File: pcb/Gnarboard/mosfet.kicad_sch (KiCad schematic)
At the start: 12 parts, among them Q1 IRF4905, Q2 MMBT5551L, U5 ACS725xLCTR-20AU

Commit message: board close to being ready for a prototype
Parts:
- added J5: Screw_Terminal_01x02, gnarboard:Amphenol OQ02715, symbol Connector:Screw_Terminal_01x02
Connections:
- net LOAD+: no longer names the net of F1.3, Q1.2 (D)
- net LOAD+: now also J5.1 (Pin_1)
- net LOAD-: no longer names the net of U5.1 (IP+), U5.2 (IP+)
- net LOAD-: now also J5.2 (Pin_2)
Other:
- moved on the sheet: C3, C4, C5, U5

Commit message: added the flyback diode
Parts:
- added D10: GS1G-LTP, Diode_SMD:D_SMA, symbol Diode:MRA4004T3G
- R4: value 10k -> 47k
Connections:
- net at F1.3, J5.1 (Pin_1), Q1.2 (D): now also D10.1 (K)
- net at J5.2 (Pin_2), U5.1 (IP+), U5.2 (IP+): now also D10.2 (A)
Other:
- moved on the sheet: J5
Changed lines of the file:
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@@
   (junction (at 167.64 113.03) (diameter 0) (color 0 0 0 0)
   )
+  (junction (at 148.59 86.36) (diameter 0) (color 0 0 0 0)
+  )
   (junction (at 107.95 76.2) (diameter 0) (color 0 0 0 0)
   )
@@
   (junction (at 139.7 72.39) (diameter 0) (color 0 0 0 0)
   )
+  (junction (at 148.59 83.82) (diameter 0) (color 0 0 0 0)
+  )
   (junction (at 139.7 54.61) (diameter 0) (color 0 0 0 0)
   )
@@
     (stroke (width 0) (type default))
   )
-  (wire (pts (xy 139.7 87.63) (xy 149.86 87.63))
+  (wire (pts (xy 139.7 83.82) (xy 148.59 83.82))
     (stroke (width 0) (type default))
   )
@@
     (stroke (width 0) (type default))
   )
-  (wire (pts (xy 139.7 90.17) (xy 139.7 107.95))
-    (stroke (width 0) (type default))
-  )
-  (wire (pts (xy 149.86 90.17) (xy 139.7 90.17))
+  (wire (pts (xy 139.7 86.36) (xy 139.7 107.95))
+    (stroke (width 0) (type default))
+  )
+  (wire (pts (xy 149.86 86.36) (xy 148.59 86.36))
     (stroke (width 0) (type default))
   )
@@
     (stroke (width 0) (type default))
   )
-  (wire (pts (xy 139.7 72.39) (xy 139.7 87.63))
+  (wire (pts (xy 139.7 72.39) (xy 139.7 83.82))
     (stroke (width 0) (type default))
   )
@@
     (stroke (width 0) (type default))
   )
+  (wire (pts (xy 148.59 80.01) (xy 148.59 83.82))
+    (stroke (width 0) (type default))
+  )
+  (wire (pts (xy 162.56 88.9) (xy 162.56 90.17))
+    (stroke (width 0) (type default))
+  )
   (wire (pts (xy 127 91.44) (xy 118.11 91.44))
     (stroke (width 0) (type default))
@@
     (stroke (width 0) (type default))
   )
+  (wire (pts (xy 148.59 90.17) (xy 148.59 86.36))
+    (stroke (width 0) (type default))
+  )
+  (wire (pts (xy 162.56 90.17) (xy 148.59 90.17))
+    (stroke (width 0) (type default))
+  )
   (wire (pts (xy 160.02 124.46) (xy 167.64 124.46))
     (stroke (width 0) (type default))
@@
     (stroke (width 0) (type default))
   )
+  (wire (pts (xy 148.59 86.36) (xy 139.7 86.36))
+    (stroke (width 0) (type default))
+  )
   (wire (pts (xy 116.84 76.2) (xy 119.38 76.2))
     (stroke (width 0) (type default))
@@
     (stroke (width 0) (type default))
   )
+  (wire (pts (xy 162.56 81.28) (xy 162.56 80.01))
+    (stroke (width 0) (type default))
+  )
   (wire (pts (xy 128.27 62.23) (xy 128.27 63.5))
     (stroke (width 0) (type default))
@@
     (stroke (width 0) (type default))
   )
+  (wire (pts (xy 162.56 80.01) (xy 148.59 80.01))
+    (stroke (width 0) (type default))
+  )
   (wire (pts (xy 128.27 71.12) (xy 128.27 69.85))
     (stroke (width 0) (type default))
@@
   )
   (wire (pts (xy 160.02 113.03) (xy 167.64 113.03))
+    (stroke (width 0) (type default))
+  )
+  (wire (pts (xy 148.59 83.82) (xy 149.86 83.82))
     (stroke (width 0) (type default))
   )
@@
     )
   )
+  (symbol (lib_id "Diode:MRA4004T3G") (at 162.56 85.09 270) (unit 1)
+    (in_bom yes) (on_board yes) (dnp no) (fields_autoplaced)
+    (property "Reference" "D10" (at 165.1 83.82 90)
+      (effects (font (size 1.27 1.27)) (justify left))
+    )
+    (property "Value" "GS1G-LTP" (at 165.1 86.36 90)
+      (effects (font (size 1.27 1.27)) (justify left))
+    )
+    (property "Footprint" "Diode_SMD:D_SMA" (at 158.115 85.09 0)
+      (effects (font (size 1.27 1.27)) hide)
+    )
+    (property "Datasheet" "http://www.onsemi.com/pub_link/Collateral/MRA4003T3-D.PDF" (at 162.56 85.09 0)
+      (effects (font (size 1.27 1.27)) hide)
+    )
+    (property "Sim.Device" "D" (at 162.56 85.09 0)
+      (effects (font (size 1.27 1.27)) hide)
+    )
+    (property "Sim.Pins" "1=K 2=A" (at 162.56 85.09 0)
+      (effects (font (size 1.27 1.27)) hide)
+    )
+    (pin "1")
+    (pin "2")
+    (instances
+      (project "Gnarboard"
+        (path "/c83c6236-96e9-46ad-9d7a-9e2efa4a7966/0eec6767-666b-42c0-ba36-2a83c9caeade"
+          (reference "D10") (unit 1)
+        )
+        (path "/c83c6236-96e9-46ad-9d7a-9e2efa4a7966/ccdb1c25-8d0f-4f30-ab70-bbc1ecf3f6f7"
+          (reference "D11") (unit 1)
+        )
+        (path "/c83c6236-96e9-46ad-9d7a-9e2efa4a7966/1e692482-a022-407a-8cb5-d9a3b23521a6"
+          (reference "D12") (unit 1)
+        )
+        (path "/c83c6236-96e9-46ad-9d7a-9e2efa4a7966/5952e660-2bb6-45cf-b9ea-f7a7c2d0954e"
+          (reference "D13") (unit 1)
+        )
+        (path "/c83c6236-96e9-46ad-9d7a-9e2efa4a7966/772d44f5-8758-48db-a140-72ed8e75e88c"
+          (reference "D14") (unit 1)
+        )
+        (path "/c83c6236-96e9-46ad-9d7a-9e2efa4a7966/424e7b24-5644-46f2-85bb-1e459a343705"
+          (reference "D15") (unit 1)
+        )
+        (path "/c83c6236-96e9-46ad-9d7a-9e2efa4a7966/4c1df725-56ca-4be4-8107-a39054acbca4"
+          (reference "D16") (unit 1)
+        )
+        (path "/c83c6236-96e9-46ad-9d7a-9e2efa4a7966/a8a81147-5613-4820-beb3-a7ca76d0db8e"
+          (reference "D17") (unit 1)
+        )
+      )
+    )
+  )
   (symbol (lib_id "Device:R_Small_US") (at 107.95 80.01 180) (unit 1)
     (in_bom yes) (on_board yes) (dnp no) (fields_autoplaced)
@@
       (effects (font (size 1.27 1.27)) (justify right))
     )
-    (property "Value" "10k" (at 130.81 60.96 0)
+    (property "Value" "47k" (at 130.81 60.96 0)
       (effects (font (size 1.27 1.27)) (justify right))
     )
@@
     )
   )
-  (symbol (lib_id "Connector:Screw_Terminal_01x02") (at 154.94 87.63 0) (unit 1)
-    (in_bom yes) (on_board yes) (dnp no) (fields_autoplaced)
-    (property "Reference" "J5" (at 157.48 87.63 0)
-      (effects (font (size 1.27 1.27)) (justify left))
-    )
-    (property "Value" "Screw_Terminal_01x02" (at 157.48 90.17 0)
+  (symbol (lib_id "Connector:Screw_Terminal_01x02") (at 154.94 83.82 0) (unit 1)
+    (in_bom yes) (on_board yes) (dnp no) (fields_autoplaced)
+    (property "Reference" "J5" (at 157.48 83.82 0)
+      (effects (font (size 1.27 1.27)) (justify left))
+    )
+    (property "Value" "Screw_Terminal_01x02" (at 157.48 86.36 0)
       (effects (font (size 1.27 1.27)) (justify left) hide)
     )
-    (property "Footprint" "gnarboard:Amphenol OQ02715" (at 154.94 87.63 0)
-      (effects (font (size 1.27 1.27)) hide)
-    )
-    (property "Datasheet" "~" (at 154.94 87.63 0)
-      (effects (font (size 1.27 1.27)) hide)
-    )
+    (property "Footprint" "gnarboard:Amphenol OQ02715" (at 154.94 83.82 0)
+      (effects (font (size 1.27 1.27)) hide)
+    )
+    (property "Datasheet" "~" (at 154.94 83.82 0)
+      (effects (font (size 1.27 1.27)) hide)
+    )

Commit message: bill of materials updated.
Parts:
- C3: Vendor (none) -> C0805C102J1HACTU
- C4: Vendor (none) -> C0805C472K5RAC
- C5: Vendor (none) -> 08053C104KAT4A
- D10, F1: Vendor (none) -> 833-GS1G-LTP
- D2: Vendor (none) -> 150080RS75000
- J5: Vendor (none) -> OQ0271500000G, TJ0271500000G
- Q1: Vendor (none) -> 942-IRF4905STRLPBF
- Q2: Vendor (none) -> 637-MMBT5551
- R1: Vendor (none) -> 652-CR0805JW-103ELF
- R2: Vendor (none) -> 652-CR0805JW-102ELF
- R3: Vendor (none) -> 652-CR0805JW-104ELF
- R4: Vendor (none) -> 652-CR0805JW-473ELF
- U5: Vendor (none) -> 250-725LLCTR20AUT
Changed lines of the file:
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@@
+      (effects (font (size 1.27 1.27)) hide)
+    )
+    (property "Vendor" " 652-CR0805JW-103ELF " (at 114.3 76.2 0)
       (effects (font (size 1.27 1.27)) hide)
     )
@@
     )
     (property "Sim.Pins" "1=K 2=A" (at 162.56 85.09 0)
+      (effects (font (size 1.27 1.27)) hide)
+    )
+    (property "Vendor" "833-GS1G-LTP" (at 162.56 85.09 0)
       (effects (font (size 1.27 1.27)) hide)
     )
@@
       (effects (font (size 1.27 1.27)) hide)
     )
+    (property "Vendor" " 652-CR0805JW-102ELF " (at 107.95 80.01 0)
+      (effects (font (size 1.27 1.27)) hide)
+    )
     (pin "1")
     (pin "2")
@@
       (effects (font (size 1.27 1.27)) hide)
     )
+    (property "Vendor" "652-CR0805JW-473ELF" (at 128.27 59.69 0)
+      (effects (font (size 1.27 1.27)) hide)
+    )
     (pin "1")
     (pin "2")
@@
     )
     (property "Datasheet" "~" (at 153.67 60.96 0)
+      (effects (font (size 1.27 1.27)) hide)
+    )
+    (property "Vendor" "833-GS1G-LTP" (at 154.94 64.77 0)
       (effects (font (size 1.27 1.27)) hide)
     )
@@
       (effects (font (size 1.27 1.27)) hide)
     )
+    (property "Vendor" "150080RS75000" (at 107.95 86.36 0)
+      (effects (font (size 1.27 1.27)) hide)
+    )
     (pin "1")
     (pin "2")
@@
       (effects (font (size 1.27 1.27)) hide)
     )
+    (property "Vendor" "08053C104KAT4A" (at 167.64 106.68 0)
+      (effects (font (size 1.27 1.27)) hide)
+    )
     (pin "1")
     (pin "2")
@@
     )
     (property "Datasheet" "~" (at 167.64 119.38 0)
+      (effects (font (size 1.27 1.27)) hide)
+    )
+    (property "Vendor" "C0805C472K5RAC" (at 167.64 119.38 0)
       (effects (font (size 1.27 1.27)) hide)
     )
@@
       (effects (font (size 1.27 1.27)) hide)
     )
+    (property "Vendor" "OQ0271500000G, TJ0271500000G" (at 154.94 83.82 0)
+      (effects (font (size 1.27 1.27)) hide)
+    )
     (pin "1")
     (pin "2")
@@
     )
     (property "Datasheet" "http://www.allegromicro.com/~/media/Files/Datasheets/ACS725-Datasheet.ashx?la=en" (at 149.86 113.03 0)
+      (effects (font (size 1.27 1.27)) hide)
+    )
+    (property "Vendor" "250-725LLCTR20AUT" (at 149.86 113.03 0)
       (effects (font (size 1.27 1.27)) hide)
     )
@@
       (effects (font (size 1.27 1.27)) hide)
     )
+    (property "Vendor" "652-CR0805JW-104ELF" (at 128.27 67.31 0)
+      (effects (font (size 1.27 1.27)) hide)
+    )
     (pin "1")
     (pin "2")
@@
     )
     (property "Datasheet" "~" (at 160.02 119.38 0)
+      (effects (font (size 1.27 1.27)) hide)
+    )
+    (property "Vendor" "C0805C102J1HACTU" (at 160.02 119.38 0)
       (effects (font (size 1.27 1.27)) hide)
     )
@@
       (effects (font (size 1.27 1.27)) (justify left) hide)
     )
+    (property "Vendor" " 942-IRF4905STRLPBF " (at 137.16 63.5 0)
+      (effects (font (size 1.27 1.27)) hide)
+    )
     (pin "1")
     (pin "2")
@@
       (effects (font (size 1.27 1.27)) (justify left) hide)
     )
-    (pin "1")
+    (property "Vendor" "637-MMBT5551" (at 124.46 76.2 0)
+      (effects (font (size 1.27 1.27)) hide)
+    )
+    (pin "1")

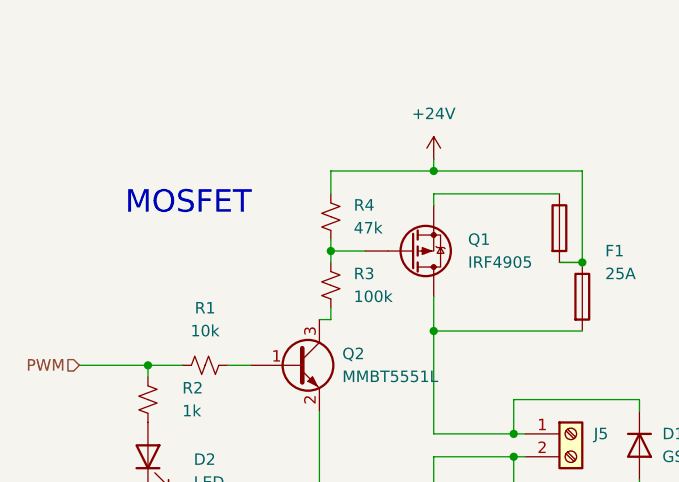
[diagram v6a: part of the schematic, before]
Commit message: got the mosfet driver circuit sorted - zener to the rescue.  also added the CAN/N2K header.
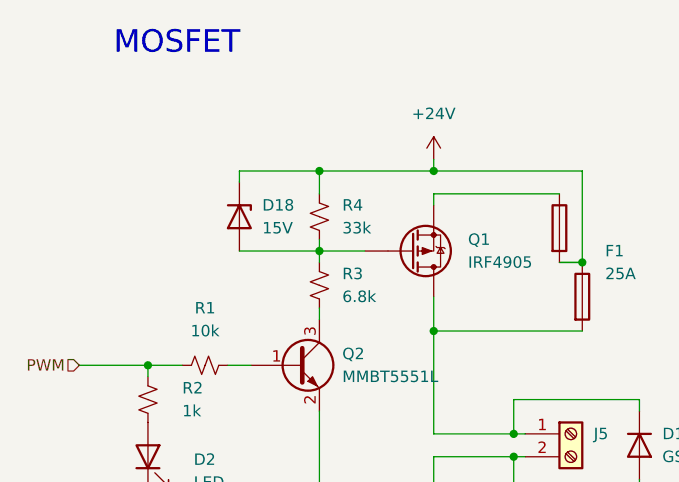
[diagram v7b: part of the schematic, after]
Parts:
- added D18: 15V, Diode_SMD:D_SOD-323_HandSoldering, symbol Device:D_Zener
- R3: value 100k -> 6.8k
- R4: value 47k -> 33k
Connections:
- net +24V: now also D18.1 (K)
- net at Q1.1 (G), R3.2, R4.1: now also D18.2 (A)
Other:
- moved on the sheet: R3, R4
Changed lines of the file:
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@@
   (junction (at 148.59 83.82) (diameter 0) (color 0 0 0 0)
   )
+  (junction (at 127 54.61) (diameter 0) (color 0 0 0 0)
+  )
   (junction (at 139.7 54.61) (diameter 0) (color 0 0 0 0)
   )
-  (junction (at 128.27 63.5) (diameter 0) (color 0 0 0 0)
+  (junction (at 127 63.5) (diameter 0) (color 0 0 0 0)
   )
   (wire (pts (xy 160.02 115.57) (xy 160.02 116.84))
@@
     (stroke (width 0) (type default))
   )
-  (wire (pts (xy 128.27 57.15) (xy 128.27 54.61))
+  (wire (pts (xy 127 57.15) (xy 127 54.61))
     (stroke (width 0) (type default))
   )
@@
     (stroke (width 0) (type default))
   )
-  (wire (pts (xy 128.27 71.12) (xy 127 71.12))
-    (stroke (width 0) (type default))
-  )
   (wire (pts (xy 161.29 102.87) (xy 161.29 106.68))
     (stroke (width 0) (type default))
@@
     (stroke (width 0) (type default))
   )
-  (wire (pts (xy 128.27 63.5) (xy 128.27 64.77))
+  (wire (pts (xy 127 63.5) (xy 127 64.77))
     (stroke (width 0) (type default))
   )
@@
     (stroke (width 0) (type default))
   )
-  (wire (pts (xy 128.27 63.5) (xy 132.08 63.5))
+  (wire (pts (xy 127 63.5) (xy 132.08 63.5))
     (stroke (width 0) (type default))
   )
@@
     (stroke (width 0) (type default))
   )
-  (wire (pts (xy 128.27 54.61) (xy 139.7 54.61))
+  (wire (pts (xy 127 54.61) (xy 139.7 54.61))
+    (stroke (width 0) (type default))
+  )
+  (wire (pts (xy 118.11 54.61) (xy 118.11 55.88))
     (stroke (width 0) (type default))
   )
@@
     (stroke (width 0) (type default))
   )
-  (wire (pts (xy 128.27 62.23) (xy 128.27 63.5))
+  (wire (pts (xy 127 62.23) (xy 127 63.5))
     (stroke (width 0) (type default))
   )
@@
     (stroke (width 0) (type default))
   )
+  (wire (pts (xy 127 54.61) (xy 118.11 54.61))
+    (stroke (width 0) (type default))
+  )
   (wire (pts (xy 162.56 80.01) (xy 148.59 80.01))
     (stroke (width 0) (type default))
   )
-  (wire (pts (xy 128.27 71.12) (xy 128.27 69.85))
+  (wire (pts (xy 127 71.12) (xy 127 69.85))
+    (stroke (width 0) (type default))
+  )
+  (wire (pts (xy 118.11 63.5) (xy 127 63.5))
     (stroke (width 0) (type default))
   )
@@
     (effects (font (size 2.5 2.5)) (justify left bottom))
   )
-  (text "MOSFET" (at 105.41 59.69 0)
+  (text "MOSFET" (at 104.14 41.91 0)
     (effects (font (size 2.5 2.5)) (justify left bottom))
   )
@@
     )
   )
-  (symbol (lib_id "Device:R_Small_US") (at 128.27 59.69 180) (unit 1)
-    (in_bom yes) (on_board yes) (dnp no) (fields_autoplaced)
-    (property "Reference" "R4" (at 130.81 58.42 0)
+  (symbol (lib_id "Device:R_Small_US") (at 127 59.69 180) (unit 1)
+    (in_bom yes) (on_board yes) (dnp no) (fields_autoplaced)
+    (property "Reference" "R4" (at 129.54 58.42 0)
       (effects (font (size 1.27 1.27)) (justify right))
     )
-    (property "Value" "47k" (at 130.81 60.96 0)
+    (property "Value" "33k" (at 129.54 60.96 0)
       (effects (font (size 1.27 1.27)) (justify right))
     )
-    (property "Footprint" "Resistor_SMD:R_0805_2012Metric_Pad1.20x1.40mm_HandSolder" (at 128.27 59.69 0)
-      (effects (font (size 1.27 1.27)) hide)
-    )
-    (property "Datasheet" "~" (at 128.27 59.69 0)
-      (effects (font (size 1.27 1.27)) hide)
-    )
-    (property "Vendor" "652-CR0805JW-473ELF" (at 128.27 59.69 0)
+    (property "Footprint" "Resistor_SMD:R_0805_2012Metric_Pad1.20x1.40mm_HandSolder" (at 127 59.69 0)
+      (effects (font (size 1.27 1.27)) hide)
+    )
+    (property "Datasheet" "~" (at 127 59.69 0)
+      (effects (font (size 1.27 1.27)) hide)
+    )
+    (property "Vendor" "652-CR0805JW-473ELF" (at 127 59.69 0)
       (effects (font (size 1.27 1.27)) hide)
     )
@@
     )
   )
-  (symbol (lib_id "Device:R_Small_US") (at 128.27 67.31 180) (unit 1)
-    (in_bom yes) (on_board yes) (dnp no) (fields_autoplaced)
-    (property "Reference" "R3" (at 130.81 66.04 0)
+  (symbol (lib_id "Device:R_Small_US") (at 127 67.31 180) (unit 1)
+    (in_bom yes) (on_board yes) (dnp no) (fields_autoplaced)
+    (property "Reference" "R3" (at 129.54 66.04 0)
       (effects (font (size 1.27 1.27)) (justify right))
     )
-    (property "Value" "100k" (at 130.81 68.58 0)
+    (property "Value" "6.8k" (at 129.54 68.58 0)
       (effects (font (size 1.27 1.27)) (justify right))
     )
-    (property "Footprint" "Resistor_SMD:R_0805_2012Metric_Pad1.20x1.40mm_HandSolder" (at 128.27 67.31 0)
-      (effects (font (size 1.27 1.27)) hide)
-    )
-    (property "Datasheet" "~" (at 128.27 67.31 0)
-      (effects (font (size 1.27 1.27)) hide)
-    )
-    (property "Vendor" "652-CR0805JW-104ELF" (at 128.27 67.31 0)
+    (property "Footprint" "Resistor_SMD:R_0805_2012Metric_Pad1.20x1.40mm_HandSolder" (at 127 67.31 0)
+      (effects (font (size 1.27 1.27)) hide)
+    )
+    (property "Datasheet" "~" (at 127 67.31 0)
+      (effects (font (size 1.27 1.27)) hide)
+    )
+    (property "Vendor" "652-CR0805JW-104ELF" (at 127 67.31 0)
       (effects (font (size 1.27 1.27)) hide)
     )
@@
         )
       )
+    )
+  )
+  (symbol (lib_id "Device:D_Zener") (at 118.11 59.69 270) (unit 1)
+    (in_bom yes) (on_board yes) (dnp no) (fields_autoplaced)
+    (property "Reference" "D18" (at 120.65 58.42 90)
+      (effects (font (size 1.27 1.27)) (justify left))
+    )
+    (property "Value" "15V" (at 120.65 60.96 90)
+      (effects (font (size 1.27 1.27)) (justify left))
+    )
+    (property "Footprint" "Diode_SMD:D_SOD-323_HandSoldering" (at 118.11 59.69 0)
+      (effects (font (size 1.27 1.27)) hide)
+    )
+    (property "Datasheet" "~" (at 118.11 59.69 0)
+      (effects (font (size 1.27 1.27)) hide)
+    )
+    (property "Vendor" "771-BZX384-C15115" (at 118.11 59.69 90)
+      (effects (font (size 1.27 1.27)) hide)
+    )
+    (pin "1")
+    (pin "2")
+    (instances
+      (project "Gnarboard"
+        (path "/c83c6236-96e9-46ad-9d7a-9e2efa4a7966/0eec6767-666b-42c0-ba36-2a83c9caeade"
+          (reference "D18") (unit 1)
+        )
+        (path "/c83c6236-96e9-46ad-9d7a-9e2efa4a7966/ccdb1c25-8d0f-4f30-ab70-bbc1ecf3f6f7"
+          (reference "D19") (unit 1)
+        )
+        (path "/c83c6236-96e9-46ad-9d7a-9e2efa4a7966/1e692482-a022-407a-8cb5-d9a3b23521a6"
+          (reference "D20") (unit 1)
+        )
+        (path "/c83c6236-96e9-46ad-9d7a-9e2efa4a7966/5952e660-2bb6-45cf-b9ea-f7a7c2d0954e"
+          (reference "D21") (unit 1)
+        )
+        (path "/c83c6236-96e9-46ad-9d7a-9e2efa4a7966/772d44f5-8758-48db-a140-72ed8e75e88c"
+          (reference "D22") (unit 1)
+        )
+        (path "/c83c6236-96e9-46ad-9d7a-9e2efa4a7966/424e7b24-5644-46f2-85bb-1e459a343705"
+          (reference "D23") (unit 1)
+        )
+        (path "/c83c6236-96e9-46ad-9d7a-9e2efa4a7966/4c1df725-56ca-4be4-8107-a39054acbca4"
+          (reference "D24") (unit 1)
+        )
+        (path "/c83c6236-96e9-46ad-9d7a-9e2efa4a7966/a8a81147-5613-4820-beb3-a7ca76d0db8e"
+          (reference "D25") (unit 1)
+        )
+      )

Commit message: a couple tweaks to the board
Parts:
- R3: Vendor 652-CR0805JW-104ELF -> 652-CR0805JW-682ELF
- R4: Vendor 652-CR0805JW-473ELF -> 652-CR0805JW-333ELF
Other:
- moved on the sheet: D18, D2, Q2, R1, R2, R3, R4
